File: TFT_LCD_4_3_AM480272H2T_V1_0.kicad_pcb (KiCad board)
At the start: 2 copper layers, 67.5 x 105.7 mm, 23 parts, among them P1 HRS_FH28, P2 40pin_fpc_top_0_5mm, P3 4pin_Joint_Tech_0_5mm, P4 4pin_Cvilux_1_0mm, U1 LM27313

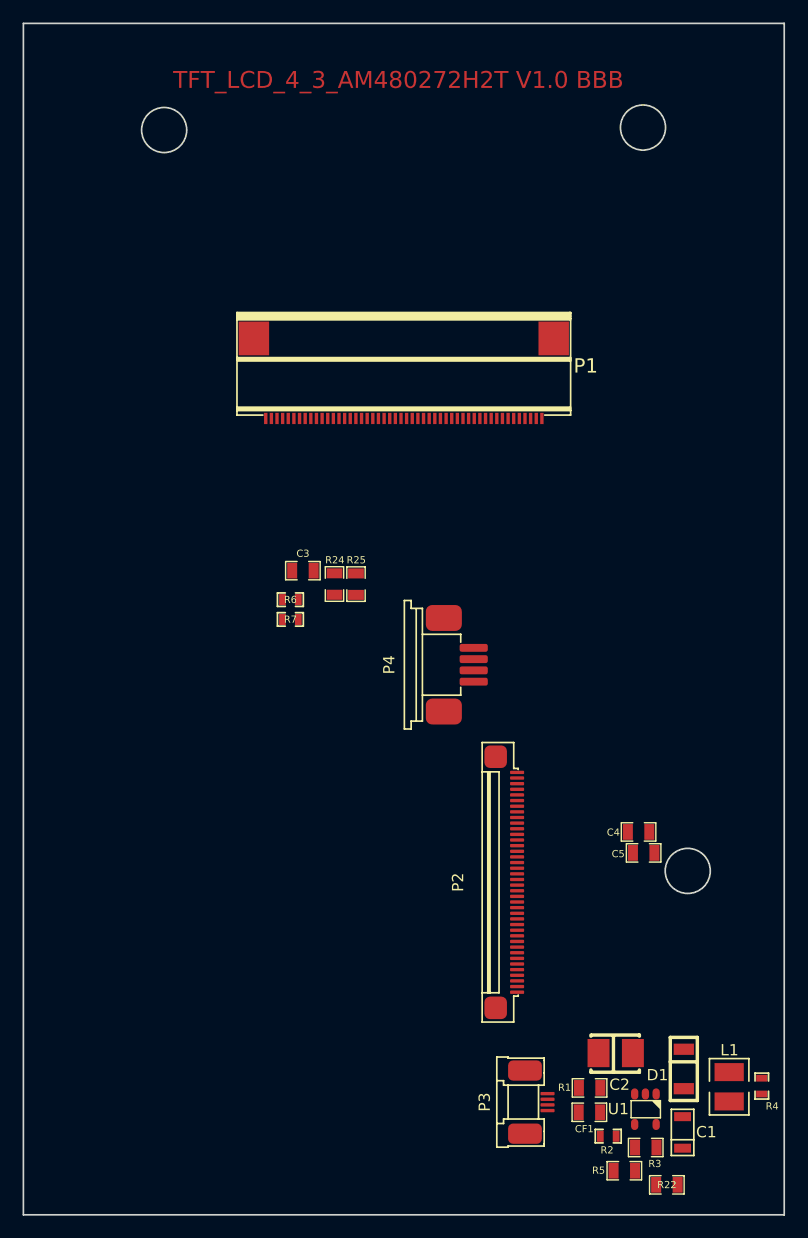
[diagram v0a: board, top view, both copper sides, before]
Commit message: Schematic finished, needes to be rechecked, pcb finished needes to be tweeked
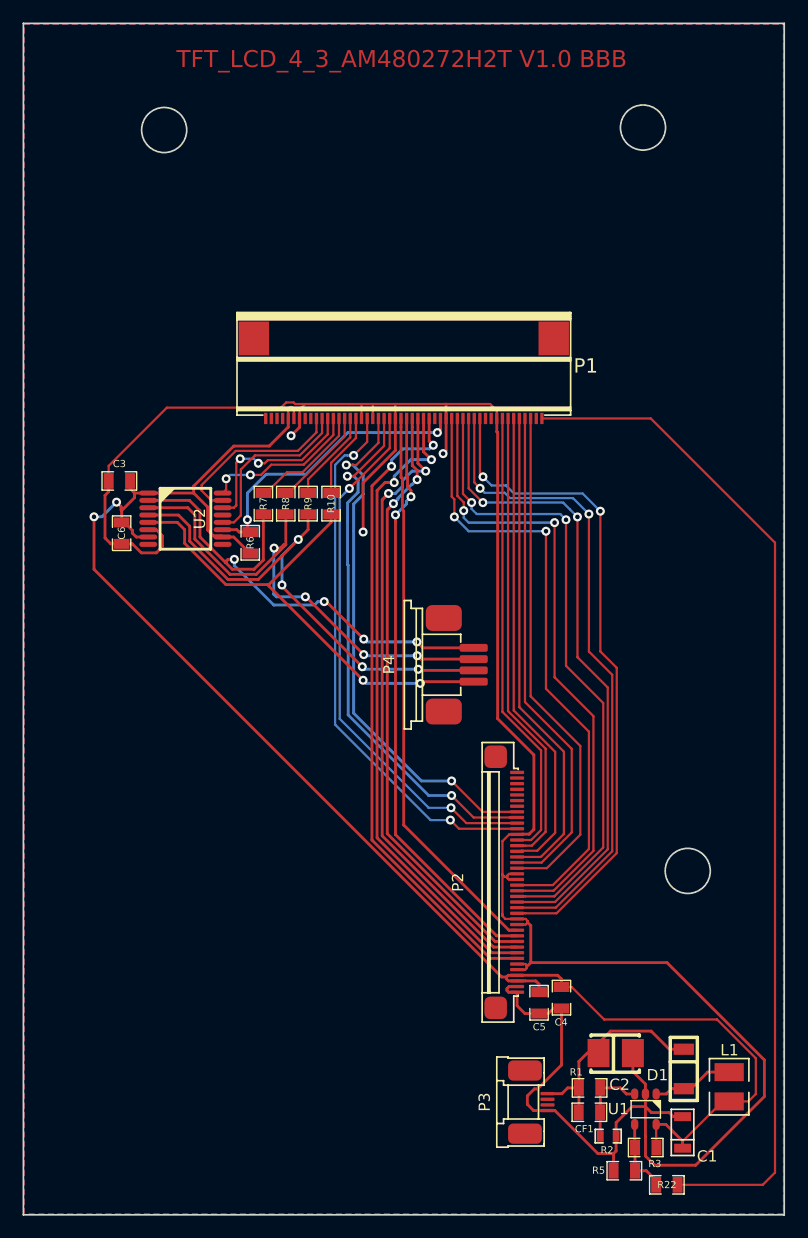
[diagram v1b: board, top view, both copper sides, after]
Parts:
- removed R24, R25: 4K7_0805, Resistor_Smd_0805:4k7_0805
- removed R4: 0R_0603, Resistor_Smd_0603:0R_0603
- added C6: 100nF_0805, Capacitors_Smd_0805:100nF_0805, F.Cu at (125.7, 83.0)
- added R10: 0R_0805, Resistor_Smd_0805:0R_0805, F.Cu at (144.3, 80.4)
- added R8: 0R_0805, Resistor_Smd_0805:0R_0805, F.Cu at (140.2, 80.4)
- added R9: 0R_0805, Resistor_Smd_0805:0R_0805, F.Cu at (142.2, 80.4)
- added U2: XPT2046, Touch_Sensors:XPT2046_TSSOP16, F.Cu at (131.3, 81.7)
- R1: value 120K_0805 -> 240K_0805; footprint Resistor_Smd_0805:120k_0805 -> Resistor_Smd_0805:240k_0805
- R6: value 0R_0603 -> 47K_0805; footprint Resistor_Smd_0603:0R_0603 -> Resistor_Smd_0805:47k_0805
- R7: value 0R_0603 -> 0R_0805; footprint Resistor_Smd_0603:0R_0603 -> Resistor_Smd_0805:0R_0805
- moved C3 18.1 mm to (125.5, 78.3)
- moved C4 16.2 mm to (164.7, 124.2), turned to 270 degrees
- moved C5 16.2 mm to (162.7, 124.6), turned to 270 degrees
- moved R7 10.5 mm to (138.2, 80.4), turned to 270 degrees
- moved R6 6.17 mm to (137.1, 83.8), turned to 270 degrees
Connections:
- net LCD_RESET renamed Net-(P1-Pad2)
- net TSC_SCL renamed Net-(P1-Pad9)
- net TSC_SDA renamed Net-(P1-Pad8)
- net TSC_~RST renamed Net-(P1-Pad1)
- net TSC_~WAKE renamed TSC_BUSY
- C1 pad 1: Net-(C1-Pad1) -> 3V3
- C3 pad 2: Net-(C3-Pad2) -> 3V3
- L1 pad 1: Net-(C1-Pad1) -> 3V3
- P1 pad 10: LCD_CS -> TSC_~CS
- P1 pad 11: LCD_SDO -> TSC_DOUT
- P1 pad 12: LCD_SDI -> TSC_DI
- P1 pad 13: LCD_SCL -> TSC_DCLK
- P1 pad 3: Net-(P1-Pad3) -> (no net)
- P1 pad 4: Net-(P1-Pad4) -> (no net)
- P2 pad 34: Net-(P2-Pad34) -> (no net)
- P2 pad 35: Net-(P2-Pad35) -> (no net)
- P2 pad 36: Net-(P2-Pad36) -> (no net)
- P2 pad 37: Net-(P2-Pad37) -> (no net)
- P2 pad 38: Net-(P2-Pad38) -> (no net)
- P2 pad 39: Net-(P2-Pad39) -> (no net)
- P2 pad 40: Net-(P2-Pad40) -> (no net)
- P3 pad 1: Net-(P3-Pad1) -> LCD_DB00_B0
- P3 pad 2: Net-(P3-Pad2) -> (no net)
- P3 pad 3: Net-(P3-Pad3) -> (no net)
- P3 pad 4: Net-(P3-Pad4) -> Net-(C2-Pad1)
- R6 pad 1: LCD_LED_A -> TSC_~INT
- R6 pad 2: Net-(C2-Pad1) -> 3V3
- R7 pad 1: LCD_LED_K -> TSC_RES_ADC3
- R7 pad 2: LCD_DB00_B0 -> Net-(P4-Pad4)
- U1 pad 5: Net-(C1-Pad1) -> 3V3
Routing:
- net LCD_DB00_B0: track 0.00 -> 224.5 mm, vias 0 -> 3
- net 3V3: track 0.00 -> 142.3 mm, vias 0 -> 2
- net LCD_PWM: track 0.00 -> 90.2 mm
- net LCD_DB10_G2: track 0.00 -> 59.0 mm, vias 0 -> 2
- net LCD_DB18_R2: track 0.00 -> 58.4 mm, vias 0 -> 2
- net LCD_DB11_G3: track 0.00 -> 58.3 mm, vias 0 -> 2
- net LCD_DB19_R3: track 0.00 -> 57.7 mm, vias 0 -> 2
- net LCD_DB12_G4: track 0.00 -> 57.5 mm, vias 0 -> 2
- net LCD_DB13_G5: track 0.00 -> 57.0 mm, vias 0 -> 2
- net LCD_DB14_G6: track 0.00 -> 56.1 mm, vias 0 -> 2
- net LCD_DB20_R4: track 0.00 -> 56.0 mm, vias 0 -> 2
- net LCD_DB15_G7: track 0.00 -> 55.0 mm, vias 0 -> 2
- net LCD_DB21_R5: track 0.00 -> 53.6 mm, vias 0 -> 2
- net LCD_DB22_R6: track 0.00 -> 52.2 mm, vias 0 -> 2
- net LCD_DB23_R7: track 0.00 -> 50.1 mm
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- added copper zone on B.Cu, net LCD_DB00_B0
- added copper zone on F.Cu, net LCD_DB00_B0

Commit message: PCB tweaked, schematic still needes to be crosscheck, pcb fpc/fcc and bbb placement not checked yet
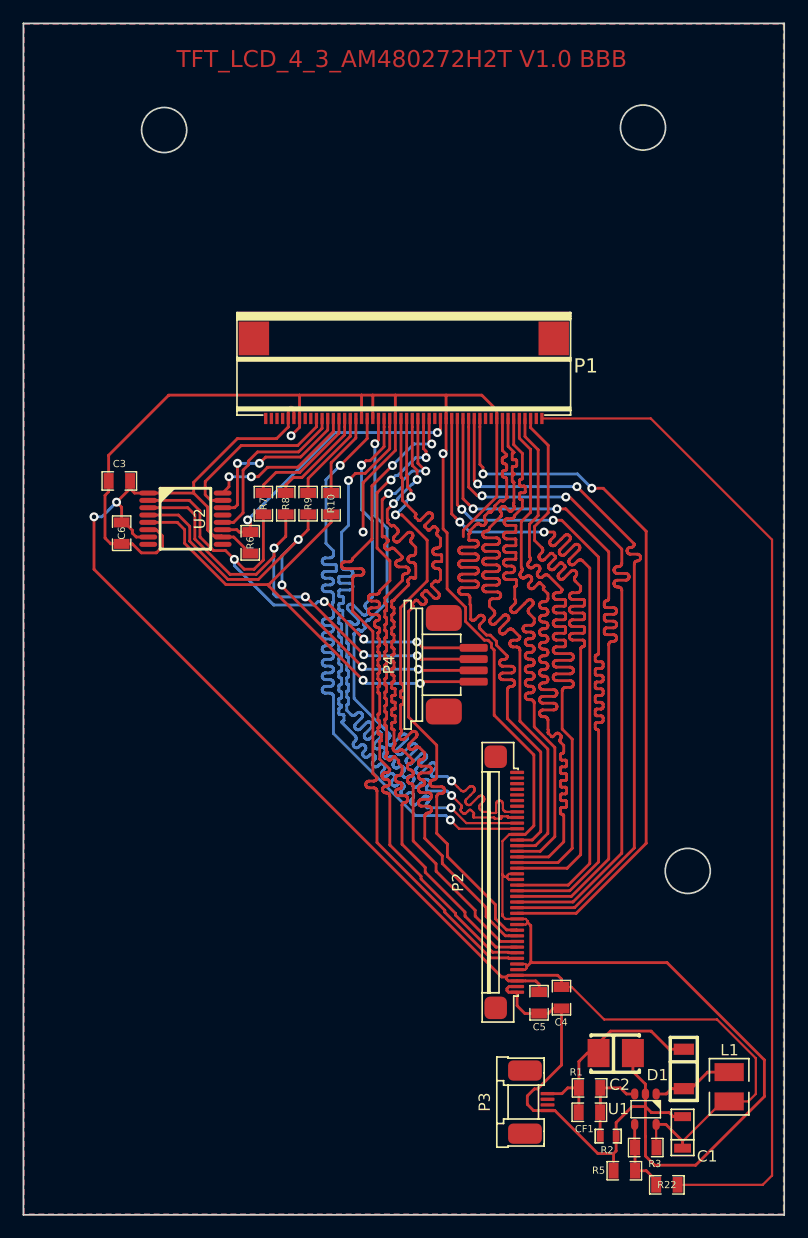
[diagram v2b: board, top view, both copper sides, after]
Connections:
- P1 pad 1: Net-(P1-Pad1) -> (no net)
- P1 pad 2: Net-(P1-Pad2) -> (no net)
- P1 pad 3: (no net) -> Net-(P1-Pad3)
- P1 pad 31: TSC_BUSY -> (no net)
- P1 pad 4: (no net) -> Net-(P1-Pad4)
- P1 pad 40: (no net) -> Net-(P1-Pad40)
- P1 pad 41: (no net) -> Net-(P1-Pad41)
- P1 pad 49: (no net) -> Net-(P1-Pad49)
- P1 pad 8: Net-(P1-Pad8) -> (no net)
- P1 pad 9: Net-(P1-Pad9) -> (no net)
- P2 pad 34: (no net) -> Net-(P2-Pad34)
- P2 pad 35: (no net) -> Net-(P2-Pad35)
- P2 pad 36: (no net) -> Net-(P2-Pad36)
- P2 pad 37: (no net) -> Net-(P2-Pad37)
- P2 pad 38: (no net) -> Net-(P2-Pad38)
- P2 pad 39: (no net) -> Net-(P2-Pad39)
- P2 pad 40: (no net) -> Net-(P2-Pad40)
- P3 pad 2: (no net) -> Net-(P3-Pad2)
- P3 pad 3: (no net) -> Net-(P3-Pad3)
- U2 pad 13: BUSY -> (no net)
- U2 pad 8: (no net) -> Net-(U2-Pad8)
- U2 pad 9: (no net) -> Net-(U2-Pad9)
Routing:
- net LCD_DB07_B7: track 40.4 -> 62.9 mm
- net LCD_DB06_B6: track 41.1 -> 63.1 mm
- net LCD_DB05_B5: track 42.3 -> 63.1 mm
- net LCD_DB04_B4: track 43.5 -> 63.5 mm
- net LCD_DB03_B3: track 44.4 -> 63.9 mm
- net LCD_DB02_B2: track 45.6 -> 62.7 mm
- net LCD_DISP: track 48.1 -> 64.2 mm
- net LCD_VSYNC: track 47.3 -> 63.3 mm
- net LCD_HSYNC: track 47.9 -> 63.6 mm
- net LCD_DB00_B0: track 224.5 -> 240.0 mm
- net LCD_DCLK: track 48.8 -> 63.6 mm
- net LCD_DB23_R7: track 50.1 -> 63.2 mm
- net LCD_DB22_R6: track 52.2 -> 63.5 mm
- net LCD_DB21_R5: track 53.6 -> 63.7 mm
- net LCD_DB15_G7: track 55.0 -> 63.6 mm
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
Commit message: Schematic crosscheck needed, FPC/FFC conntector needes to be place aligement
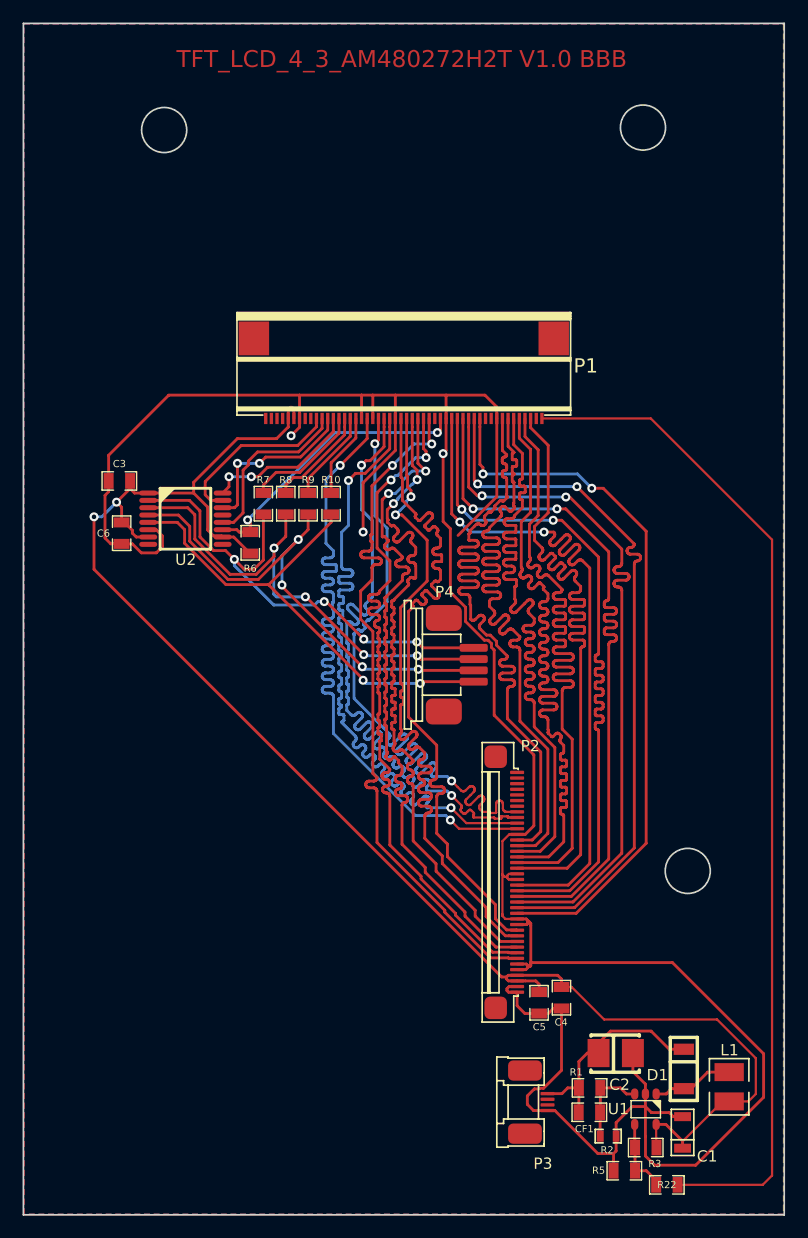
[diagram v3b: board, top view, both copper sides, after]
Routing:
- net LCD_DB00_B0: track 240.0 -> 241.2 mm
- net LCD_DB18_R2: track 63.9 -> 63.2 mm

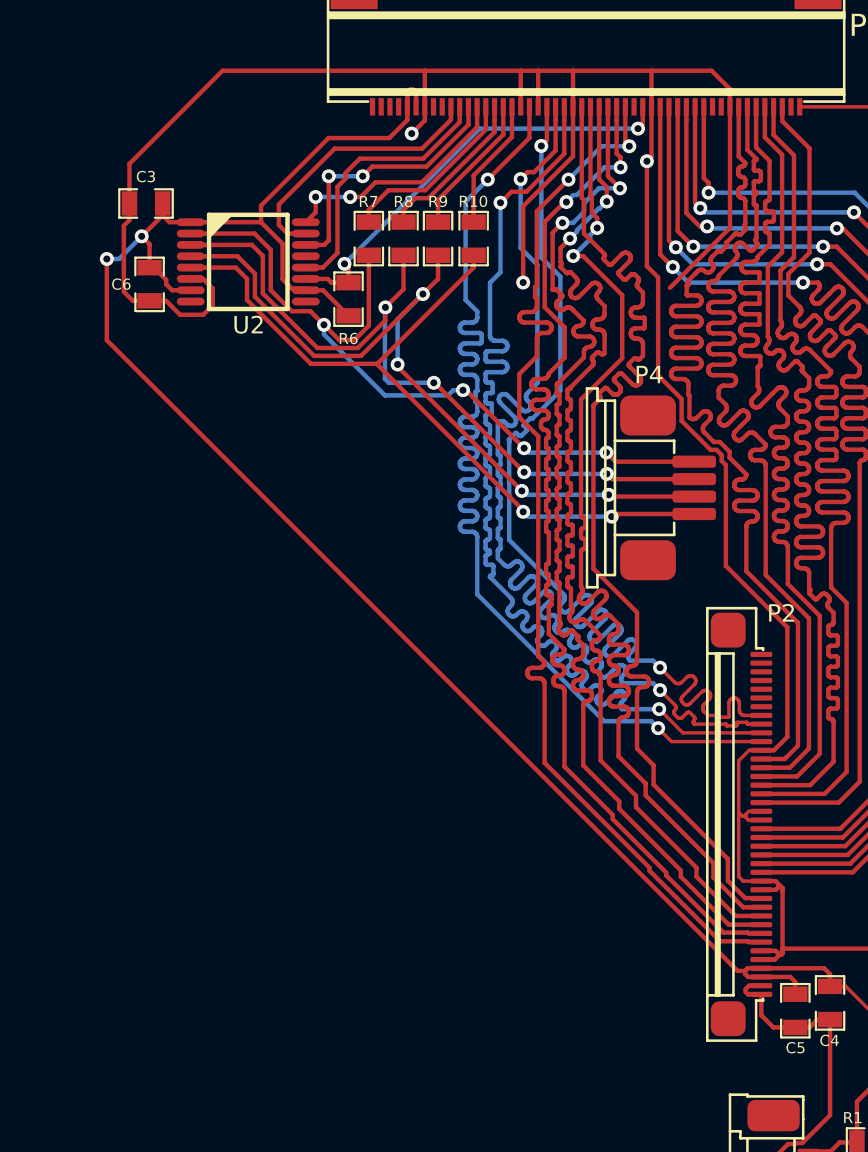
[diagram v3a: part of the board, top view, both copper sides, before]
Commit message: Corrected FPC 40pin top 0.5mm connector, generated again gerber and ps files
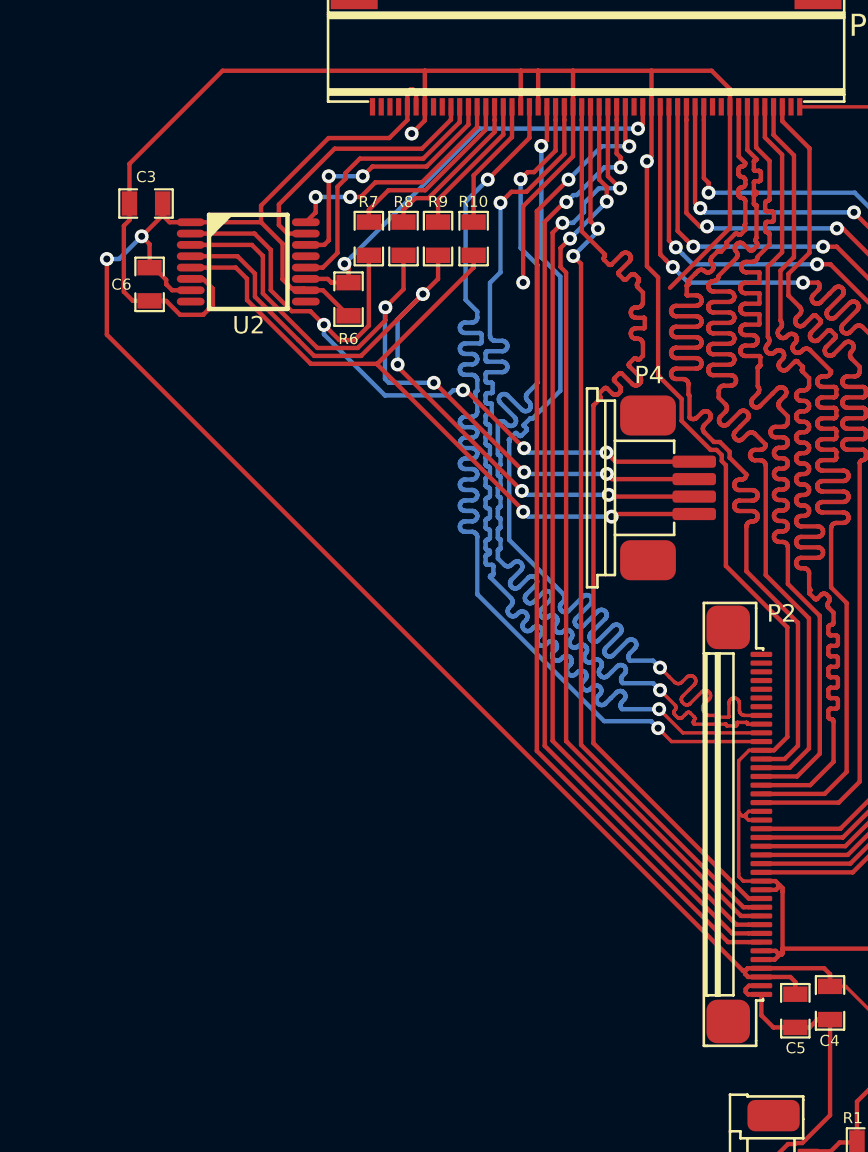
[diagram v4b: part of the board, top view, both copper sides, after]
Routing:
- net LCD_DB22_R6: track 63.5 -> 51.7 mm
- net LCD_DB21_R5: track 63.7 -> 53.1 mm
- net LCD_DB20_R4: track 64.3 -> 55.7 mm
- net LCD_DB19_R3: track 63.7 -> 56.1 mm
- net LCD_DB18_R2: track 63.2 -> 57.6 mm
- net LCD_DB23_R7: track 63.2 -> 61.3 mm
